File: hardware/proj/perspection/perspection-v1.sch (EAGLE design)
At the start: 269 parts, among them J1 MICRO-USB-10118192-0001LF, J10 1X5, J2 1X6-PTSA_1.5/6-3.5-Z, J3 1X2-PTSA_1.5/2-3.5-Z, J4 1X2-JST-PH-SMD, J5 1X2-0428202213, J6 JTAG-ARM_TC-10, J7 JTAG-ARM_TC-10, J8 1X3-0.1IN_THRUHOLE, J9 1X2-PTSA_1.5/2-3.5-Z, Q1 NMOS-CSD18533Q5A, Q10 NMOS-CSD18533Q5A, Q11 IRFML8244TRPBF, Q2 NMOS-CSD18533Q5A, Q3 NMOS-CSD18533Q5A, Q4 NMOS-CSD18533Q5A, Q5 NMOS-CSD18533Q5A, Q6 NMOS-CSD18533Q5A, Q7 NMOS-CSD18533Q5A, Q8 BSS138L, Q9 BSS138L, U1 ATUM, U10 DRV8301DCAR, U11 OPA2374AIDCNR, U12 OPA170AIDBVR, U13 BNO055, U14 TPS81256, U2 FT232RQ, U3 TPS79933DDCR, U4 MCP73831T-2ACI/OT, U5 TMS320F28069MPZT, U6 DRV8801PWPR, U7 DRV8801PWPR, U8 DRV8801PWPR, U9 DRV8801PWPR, Y1 32.768kHz

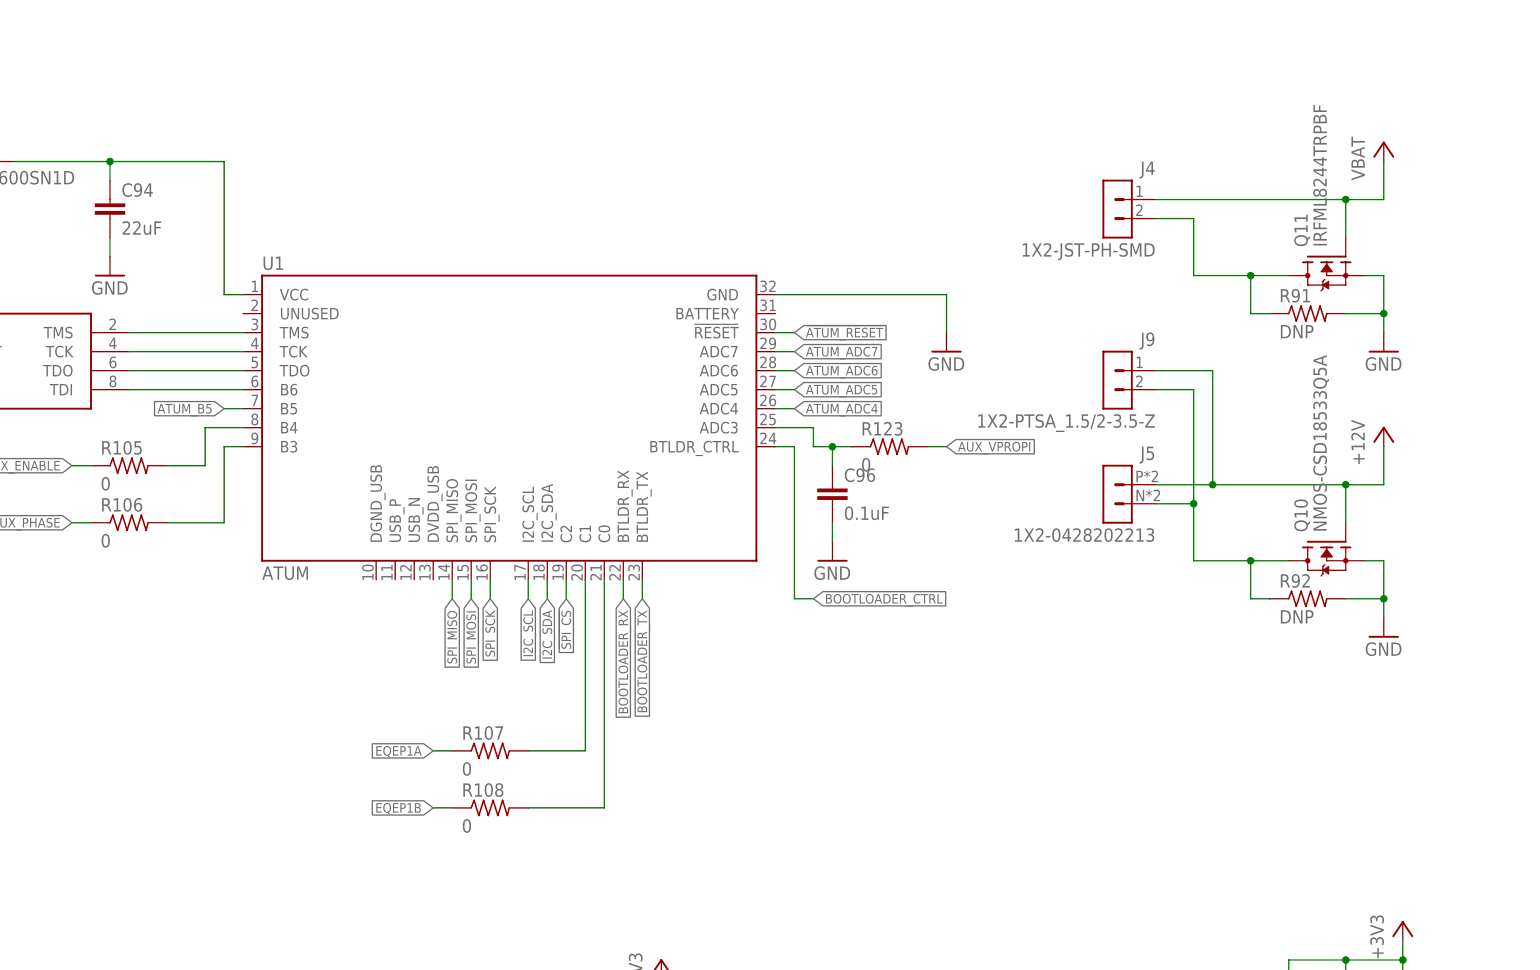
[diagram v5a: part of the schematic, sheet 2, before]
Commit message: added 4 pin connector, cleaned up test layer, added block diagram, changed GVDD cap to a larger package for higher voltage rating, removed unused cam files, added our own cam processor, added LED_PWM to atum
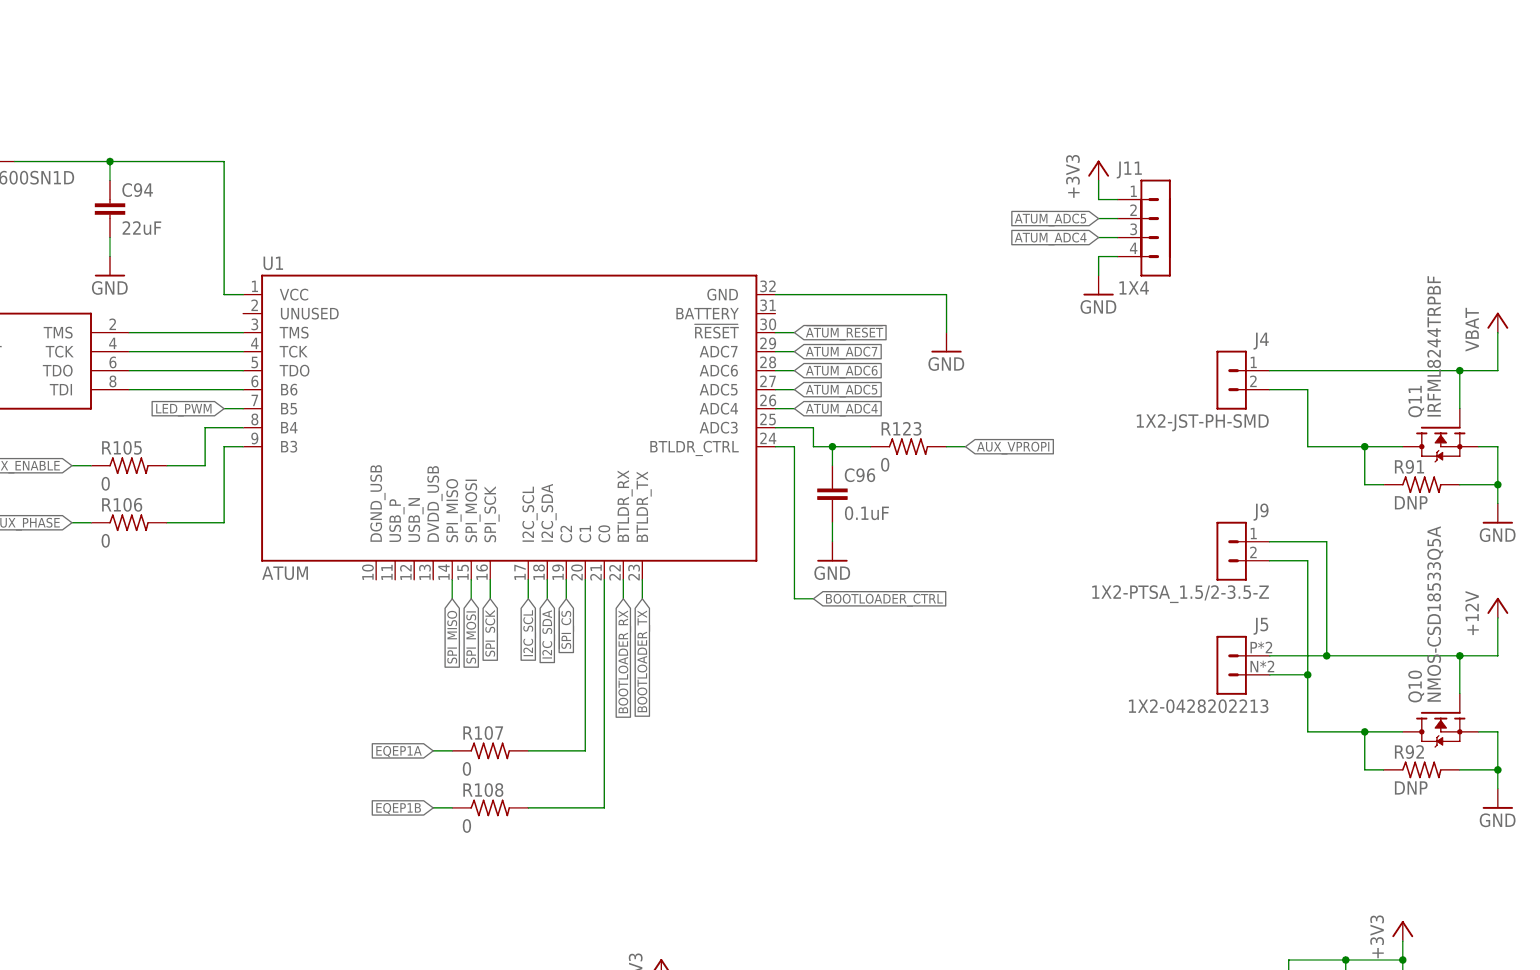
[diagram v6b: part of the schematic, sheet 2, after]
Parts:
- added J11: 1X4, perspection:1X4
- C45: device perspection:C0402 -> perspection:C0603
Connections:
- removed net ATUM_B5: U1.B5
- net +3V3: now also J11.1
- net ATUM_ADC4: now also J11.3
- net ATUM_ADC5: now also J11.2
- net GND: now also J11.4
- net LED_PWM: now also U1.B5
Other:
- note added: "12V Connector"
- note added: "3.3V Buck"
- note added: "3.3V LDO"
- note added: "5V Boost"
- note added: "ATUM"
- note added: "Brushless Motor Header"
- note added: "DRV8301"
- note added: "DRV8801"
- note added: "Encoder"
- note added: "FTDI"
- note added: "H-Bridge"
- note added: "I2C"
- note added: "IMU"
- note added: "JTAG"
- note added: "LED Drive"
- note added: "LiPo Charger"
- note added: "LiPo Connector"
- note added: "PICCOLO"
- note added: "PWM"
- note added: "PWMx4"
- note added: "Power Select"
- note added: "SPI"
- note added: "SPI+PWM"
- note added: "Terminal Block"
- note added: "Terminal Blocks"
- note added: "UART"
- note added: "USB"
- moved on the sheet: J4, J5, J9, Q10, Q11, R123, R91, R92

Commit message: ORDER THIS SHIT
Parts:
- added R124, R125, R126: 0, perspection:R0402
- R119, R121: value (none) -> 820
- R120, R122: value (none) -> 2.2k
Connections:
- removed net ATUM_ADC6: U1.ADC6
- removed net ATUM_ADC7: U1.ADC7
- new net N$50: R126.1, U5.2.GPIO31/CAN_TXA/EQEP2S/EPWM8A
- new net _PHASE1: R124.1, U5.2.GPIO51/EQEP1B/MDRA/!TZ2
- new net _PHASE2: R125.1, U5.2.GPIO50/EQEP1A/MDXA/!TZ1
- net PHASE1: now also R124.2
- net PHASE2: now also R125.2
- net PHASE3: now also R126.2
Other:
- moved on the sheet: R115, R116, R117, R118, R59, R60
